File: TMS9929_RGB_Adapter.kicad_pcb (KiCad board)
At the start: 2 copper layers, 99.1 x 45.7 mm, 59 parts, among them P1 CONN_01X06, P10 12V, P2 CONN_01X08, P3 SEL, P4 SEL, P5 SEL, P6 CONN_01X01, P7 CONN_01X01, P8 CONN_01X01, P9 CONN_01X01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

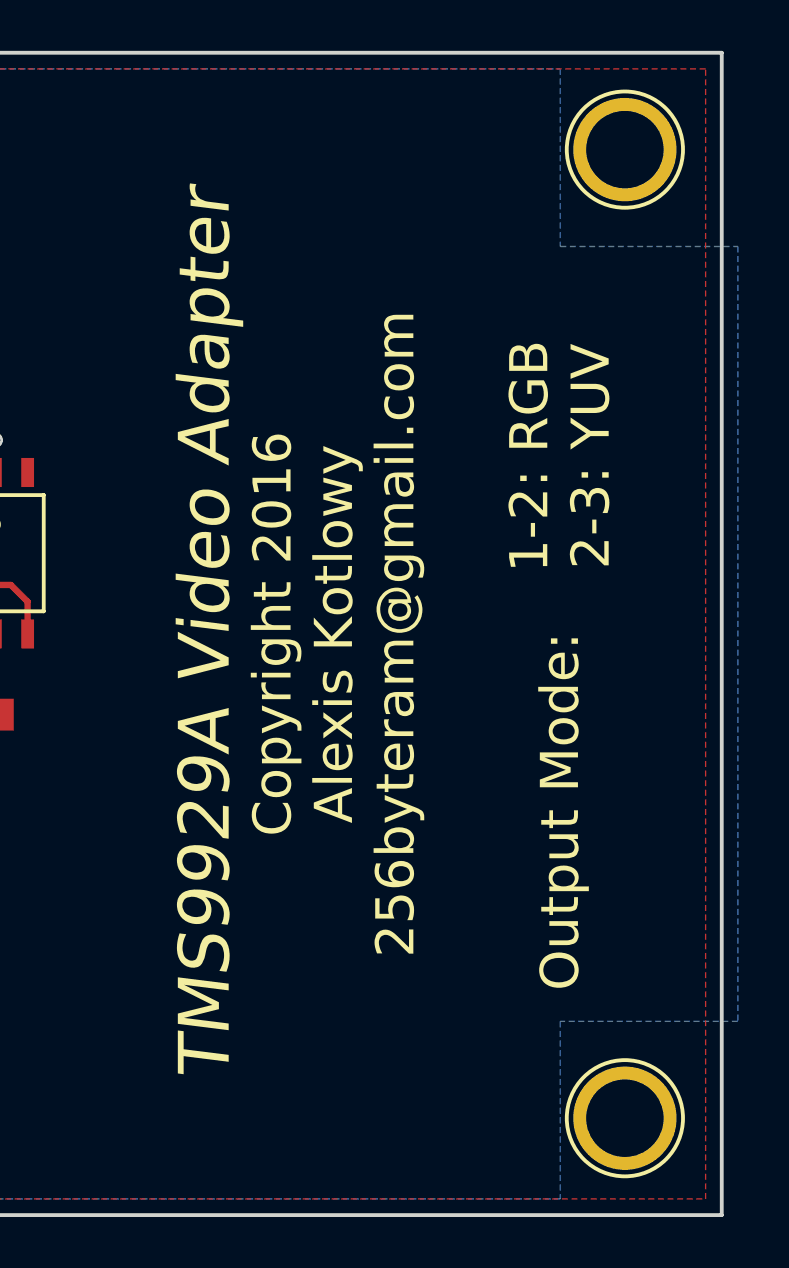
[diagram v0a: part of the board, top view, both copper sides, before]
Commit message: Initial changes to new version, copyright, DRC, etc.
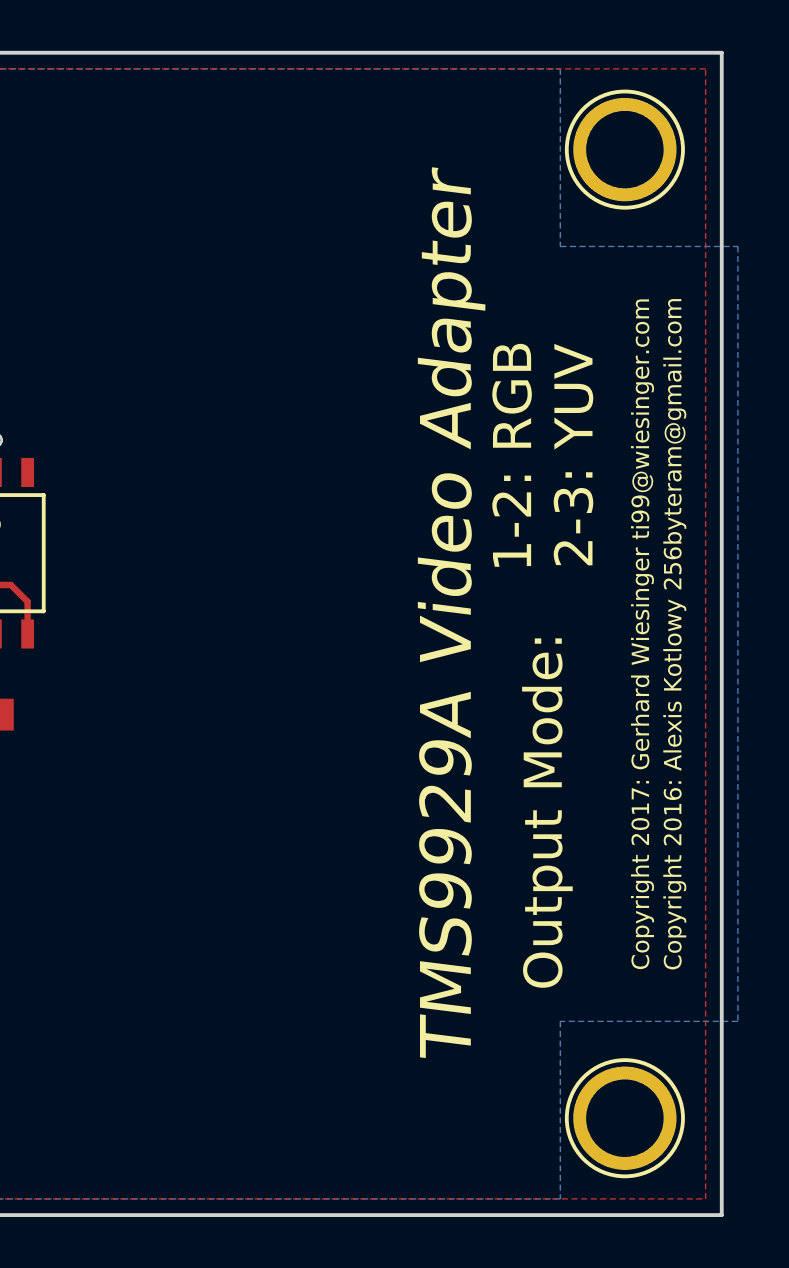
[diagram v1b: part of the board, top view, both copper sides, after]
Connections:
- P6 pad 1: (no net) -> Net-(P6-Pad1)
- P7 pad 1: (no net) -> Net-(P7-Pad1)
- P8 pad 1: (no net) -> Net-(P8-Pad1)
- P9 pad 1: (no net) -> Net-(P9-Pad1)
- U5 pad 3: (no net) -> Net-(U5-Pad3)
- U5 pad 7: (no net) -> Net-(U5-Pad7)
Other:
- net class Default: clearance 0.2 -> 0.2032; trace_width 0.25 -> 0.2286; via_dia 0.6 -> 0.6096; via_drill 0.4 -> 0.4064
- rule trace_clearance: 0.2 -> 0.2032
- rule trace_min: 0.2 -> 0.2286
- rule via_min_drill: 0.3 -> 0.3048
- rule via_min_size: 0.4 -> 0.4064
- board text added: "Copyright 2016: Alexis Kotlowy 256byteram@gmail.com"
- board text added: "Copyright 2017: Gerhard Wiesinger ti99@wiesinger.com"
- board text removed: "Copyright 2016 Alexis Kotlowy 256byteram@gmail.com"
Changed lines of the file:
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@@
-(kicad_pcb (version 4) (host pcbnew 4.0.2-stable)
+(kicad_pcb (version 4) (host pcbnew 4.0.7)
   (general
     (links 117)
     (no_connects 0)
-    (area 21.561667 19.957 123.218334 66.115001)
+    (area 21.633467 20.1038 123.146534 66.115001)
     (thickness 1.6)
-    (drawings 9)
+    (drawings 10)
     (tracks 587)
     (zones 0)
     (modules 59)
-    (nets 43)
+    (nets 49)
   )
   (page A4)
   (title_block
     (title "TMS9929A to RGB")
-    (date 2016-06-20)
+    (date 2017-09-17)
     (rev 0)
-    (company "Alexis Kotlowy")
+    (company "Gerhard Wiesinger")
+    (comment 1 "Based on: Alexis Kotlowy")
   )
   (layers
     (0 F.Cu signal)
-    (31 B.Cu signal hide)
+    (31 B.Cu signal)
     (32 B.Adhes user)
     (33 F.Adhes user)
@@
   )
   (setup
-    (last_trace_width 0.25)
-    (user_trace_width 0.5)
-    (trace_clearance 0.2)
+    (last_trace_width 0.2286)
+    (user_trace_width 0.508)
+    (trace_clearance 0.2032)
     (zone_clearance 0.508)
     (zone_45_only no)
-    (trace_min 0.2)
+    (trace_min 0.2286)
     (segment_width 0.2)
     (edge_width 0.15)
-    (via_size 0.6)
-    (via_drill 0.4)
-    (via_min_size 0.4)
-    (via_min_drill 0.3)
-    (uvia_size 0.3)
-    (uvia_drill 0.1)
+    (via_size 0.6096)
+    (via_drill 0.4064)
+    (via_min_size 0.4064)
+    (via_min_drill 0.3048)
+    (uvia_size 0.3048)
+    (uvia_drill 0.1016)
     (uvias_allowed no)
-    (uvia_min_size 0.2)
-    (uvia_min_drill 0.1)
+    (uvia_min_size 0.2032)
+    (uvia_min_drill 0.1016)
     (pcb_text_width 0.3)
     (pcb_text_size 1.5 1.5)
@@
     (pad_drill 3.048)
     (pad_to_mask_clearance 0.2)
-    (aux_axis_origin 0 0)
+    (aux_axis_origin 22.86 66.04)
+    (grid_origin 22.86 66.04)
     (visible_elements 7FFEFF7F)
     (pcbplotparams
       (layerselection 0x030f0_80000001)
-      (usegerberextensions false)
+      (usegerberextensions true)
+      (usegerberattributes true)
       (excludeedgelayer true)
-      (linewidth 0.100000)
+      (linewidth 0.101600)
       (plotframeref false)
       (viasonmask false)
       (mode 1)
-      (useauxorigin false)
+      (useauxorigin true)
       (hpglpennumber 1)
       (hpglpenspeed 20)
@@
       (plotinvisibletext false)
       (padsonsilk false)
-      (subtractmaskfromsilk false)
+      (subtractmaskfromsilk true)
       (outputformat 1)
       (mirror false)
@@
   (net 41 "Net-(R26-Pad2)")
   (net 42 "Net-(U4-Pad5)")
+  (net 43 "Net-(P6-Pad1)")
+  (net 44 "Net-(P7-Pad1)")
+  (net 45 "Net-(P8-Pad1)")
+  (net 46 "Net-(P9-Pad1)")
+  (net 47 "Net-(U5-Pad7)")
+  (net 48 "Net-(U5-Pad3)")
   (net_class Default "This is the default net class."
-    (clearance 0.2)
-    (trace_width 0.25)
-    (via_dia 0.6)
-    (via_drill 0.4)
-    (uvia_dia 0.3)
-    (uvia_drill 0.1)
+    (clearance 0.2032)
+    (trace_width 0.2286)
+    (via_dia 0.6096)
+    (via_drill 0.4064)
+    (uvia_dia 0.3048)
+    (uvia_drill 0.1016)
     (add_net /B)
     (add_net /B-Y)
@@
     (add_net "Net-(P4-Pad2)")
     (add_net "Net-(P5-Pad2)")
+    (add_net "Net-(P6-Pad1)")
+    (add_net "Net-(P7-Pad1)")
+    (add_net "Net-(P8-Pad1)")
+    (add_net "Net-(P9-Pad1)")
     (add_net "Net-(R1-Pad2)")
     (add_net "Net-(R10-Pad1)")
@@
     (add_net "Net-(R5-Pad2)")
     (add_net "Net-(U4-Pad5)")
+    (add_net "Net-(U5-Pad3)")
+    (add_net "Net-(U5-Pad7)")
     (add_net VCC)
   )
@@
     )
     (fp_circle (center 0 0) (end 0 -2.286) (layer F.SilkS) (width 0.15))
-    (pad 1 thru_hole circle (at 0 0) (size 4.064 4.064) (drill 3.048) (layers *.Mask B.Cu F.SilkS))
+    (pad 1 thru_hole circle (at 0 0) (size 4.064 4.064) (drill 3.048) (layers *.Mask B.Cu F.SilkS)
+      (net 43 "Net-(P6-Pad1)"))
   )
   (module Connect:1pin (layer F.Cu)
@@
     )
     (fp_circle (center 0 0) (end 0 -2.286) (layer F.SilkS) (width 0.15))
-    (pad 1 thru_hole circle (at 0 0) (size 4.064 4.064) (drill 3.048) (layers *.Mask B.Cu F.SilkS))
+    (pad 1 thru_hole circle (at 0 0) (size 4.064 4.064) (drill 3.048) (layers *.Mask B.Cu F.SilkS)
+      (net 45 "Net-(P8-Pad1)"))
   )
   (module Connect:1pin (layer F.Cu)
@@
     )
     (fp_circle (center 0 0) (end 0 -2.286) (layer F.SilkS) (width 0.15))
-    (pad 1 thru_hole circle (at 0 0) (size 4.064 4.064) (drill 3.048) (layers *.Mask B.Cu F.SilkS))
+    (pad 1 thru_hole circle (at 0 0) (size 4.064 4.064) (drill 3.048) (layers *.Mask B.Cu F.SilkS)
+      (net 46 "Net-(P9-Pad1)"))
   )
   (module SMD_Packages:SOIC-8-N (layer F.Cu)
@@
     (pad 8 smd rect (at -1.905 -3.175) (size 0.508 1.143) (layers F.Cu F.Paste F.Mask)
       (net 9 VCC))
-    (pad 7 smd rect (at -0.635 -3.175) (size 0.508 1.143) (layers F.Cu F.Paste F.Mask))
+    (pad 7 smd rect (at -0.635 -3.175) (size 0.508 1.143) (layers F.Cu F.Paste F.Mask)
+      (net 47 "Net-(U5-Pad7)"))
     (pad 6 smd rect (at 0.635 -3.175) (size 0.508 1.143) (layers F.Cu F.Paste F.Mask)
       (net 8 "Net-(C7-Pad1)"))
@@
     (pad 4 smd rect (at 1.905 3.175) (size 0.508 1.143) (layers F.Cu F.Paste F.Mask)
       (net 5 GND))
-    (pad 3 smd rect (at 0.635 3.175) (size 0.508 1.143) (layers F.Cu F.Paste F.Mask))
+    (pad 3 smd rect (at 0.635 3.175) (size 0.508 1.143) (layers F.Cu F.Paste F.Mask)
+      (net 48 "Net-(U5-Pad3)"))
     (pad 2 smd rect (at -0.635 3.175) (size 0.508 1.143) (layers F.Cu F.Paste F.Mask)
       (net 7 "Net-(C6-Pad2)"))
@@
     )
     (fp_circle (center 0 0) (end 0 -2.286) (layer F.SilkS) (width 0.15))
-    (pad 1 thru_hole circle (at 0 0) (size 4.064 4.064) (drill 3.048) (layers *.Mask B.Cu F.SilkS))
+    (pad 1 thru_hole circle (at 0 0) (size 4.064 4.064) (drill 3.048) (layers *.Mask B.Cu F.SilkS)
+      (net 44 "Net-(P7-Pad1)"))
   )
   (module Resistors_SMD:R_0805_HandSoldering (layer F.Cu)
@@
     )
   )
+  (gr_text "Copyright 2017: Gerhard Wiesinger ti99@wiesinger.com" (at 118.745 43.18 90) (layer F.SilkS)
+    (effects (font (size 0.681818 0.681818) (thickness 0.136364)))
+  )
   (gr_line (start 121.92 66.04) (end 121.92 20.32) (angle 90) (layer Edge.Cuts) (width 0.15))
-  (gr_text "TMS9929A Video Adapter" (at 101.6 43.18 90) (layer F.SilkS)
+  (gr_text "TMS9929A Video Adapter" (at 111.125 42.545 90) (layer F.SilkS)
     (effects (font (size 2 2) (thickness 0.5) italic))
   )
-  (gr_text "Output Mode:" (at 115.57 50.165 90) (layer F.SilkS)
+  (gr_text "Output Mode:" (at 114.935 50.165 90) (layer F.SilkS)
     (effects (font (size 1.5 1.5) (thickness 0.3)))
   )
-  (gr_text "1-2: RGB\n2-3: YUV" (at 115.57 36.195 90) (layer F.SilkS)
+  (gr_text "1-2: RGB\n2-3: YUV" (at 114.935 36.195 90) (layer F.SilkS)
     (effects (font (size 1.5 1.5) (thickness 0.3)))
   )
@@
     (effects (font (size 1.5 1.5) (thickness 0.3)))
   )
-  (gr_text "Copyright 2016\nAlexis Kotlowy\n256byteram@gmail.com" (at 106.68 43.18 90) (layer F.SilkS)
-    (effects (font (size 1.5 1.5) (thickness 0.3)))
+  (gr_text "Copyright 2016: Alexis Kotlowy 256byteram@gmail.com" (at 120.015 43.18 90) (layer F.SilkS)
+    (effects (font (size 0.681818 0.681818) (thickness 0.136364)))
   )
   (gr_line (start 22.86 66.04) (end 22.86 20.32) (angle 90) (layer Edge.Cuts) (width 0.15))
@@
         (xy 115.57 27.94) (xy 122.555 27.94) (xy 122.555 58.42) (xy 115.57 58.42) (xy 115.57 65.405)
         (xy 29.845 65.405) (xy 29.845 58.42) (xy 23.495 58.42) (xy 23.495 27.94) (xy 30.48 27.94)
-        (xy 30.48 20.955) (xy 115.57 20.955) (xy 115.57 27.94)
+        (xy 30.48 20.955) (xy 115.57 20.955)
       )
     )

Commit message: Updated schematic & PCB for added Cinch connectors as well as power supply connector and damping resistors/jumpers
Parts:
- added JDC1: Jack-DC, jack_2mm:jack_2mm, F.Cu at (124.7, 133.6)
- added JUIN1: Conn_01x02, rca_white, F.Cu at (78.0, 142.7)
- added JUOUT1: Conn_01x02, rca_white, F.Cu at (78.0, 86.9)
- added JUSHORT1: Conn_01x02, Pin_Header_Straight_1x02_Pitch2.54mm, F.Cu at (121.8, 124.7)
- added JVIN1: Conn_01x02, rca_red, F.Cu at (91.3, 142.7)
- added JVOUT1: Conn_01x02, rca_red, F.Cu at (64.6, 86.9)
- added JVSHORT1: Conn_01x02, Pin_Header_Straight_1x02_Pitch2.54mm, F.Cu at (107.3, 142.6)
- added JYIN1: Conn_01x02, rca_black, F.Cu at (64.6, 142.7)
- added JYINSHORT1: Conn_01x02, Pin_Header_Straight_1x02_Pitch2.54mm, F.Cu at (108.8, 91.6)
- added JYOUT1: Conn_01x02, rca_black, F.Cu at (91.3, 86.9)
- added RUIN1: 10E, Resistors_SMD:R_0805_HandSoldering, F.Cu at (117.3, 125.9)
- added RVIN1: 10E, Resistors_SMD:R_0805_HandSoldering, F.Cu at (106.1, 138.0)
- added RYIN1: 10E, Resistors_SMD:R_0805_HandSoldering, F.Cu at (101.8, 116.1)
- added RYIN2: 10k, Resistors_SMD:R_0805_HandSoldering, F.Cu at (99.6, 95.8)
- P1: footprint Pin_Headers:Pin_Header_Straight_1x06 -> Pin_Headers:Pin_Header_Straight_1x06_Pitch2.54mm
- P2: footprint Pin_Headers:Pin_Header_Straight_1x08 -> Pin_Headers:Pin_Header_Straight_1x08_Pitch2.54mm
- P3, P4, P5: footprint Pin_Headers:Pin_Header_Straight_1x03 -> Pin_Headers:Pin_Header_Straight_1x03_Pitch2.54mm
- moved P7 85.8 mm to (52.6, 144.0)
- moved P9 85.8 mm to (144.0, 144.0)
- moved C14 76.2 mm to (118.0, 118.0)
- moved P1 76.2 mm to (61.5, 97.0)
- moved P10 76.2 mm to (79.2, 97.0)
- moved P2 76.2 mm to (53.8, 105.9)
- moved R12 76.2 mm to (97.0, 118.0)
- moved R13 76.2 mm to (90.7, 118.0)
- moved R14 76.2 mm to (84.3, 126.9)
- moved R18 76.2 mm to (61.5, 129.4)
- moved R19 76.2 mm to (61.5, 133.9)
- moved R21 76.2 mm to (67.8, 133.9)
- moved R22 76.2 mm to (61.5, 121.8)
- moved R24 76.2 mm to (105.3, 118.0)
- moved R25 76.2 mm to (111.6, 118.0)
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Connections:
- net Net-(P1-Pad5) renamed /V
- C6 pad 1: Net-(C6-Pad1) -> /YIN
- P1 pad 3: Net-(C6-Pad1) -> /YIN
- R28 pad 2: Net-(R28-Pad2) -> Net-(JVSHORT1-Pad2)
- R29 pad 2: Net-(R29-Pad2) -> Net-(JUSHORT1-Pad2)
- U1 pad 3: Net-(C6-Pad1) -> Net-(JYINSHORT1-Pad2)
- U2 pad 3: Net-(R28-Pad2) -> Net-(JVSHORT1-Pad2)
- U3 pad 3: Net-(R29-Pad2) -> Net-(JUSHORT1-Pad2)
- U4 pad 3: Net-(R28-Pad2) -> Net-(JVSHORT1-Pad1)
- U4 pad 9: Net-(R29-Pad2) -> Net-(JUSHORT1-Pad1)
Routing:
- net /YIN: track 0.00 -> 142.3 mm, vias 0 -> 7
- net Net-(JUSHORT1-Pad2): track 0.00 -> 70.5 mm, vias 0 -> 2
- net /U: track 74.0 -> 135.6 mm, vias 1 -> 2
- net Net-(C1-Pad2): track 8.69 -> 69.9 mm
- net Net-(R29-Pad2): track 59.9 -> 0.00 mm, vias 3 -> 0
- net Net-(C3-Pad2): track 10.1 -> 67.8 mm, vias 1 -> 2
- net Net-(C6-Pad1): track 53.8 -> 0.00 mm, vias 2 -> 0
- net Net-(JYINSHORT1-Pad2): track 0.00 -> 50.1 mm, vias 0 -> 5
- net Net-(C2-Pad2): track 7.92 -> 43.3 mm
- net /V: track 70.8 -> 104.1 mm, vias 1 -> 2
- net Net-(JVSHORT1-Pad2): track 0.00 -> 26.5 mm, vias 0 -> 2
- net Net-(R28-Pad2): track 23.8 -> 0.00 mm
- net GND: track 282.4 -> 265.4 mm, vias 0 -> 2
- net Net-(JVSHORT1-Pad1): track 0.00 -> 14.4 mm
- net Net-(JUSHORT1-Pad1): track 0.00 -> 12.5 mm
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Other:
- board size 99.1 x 45.7 mm -> 99.1 x 66 mm
